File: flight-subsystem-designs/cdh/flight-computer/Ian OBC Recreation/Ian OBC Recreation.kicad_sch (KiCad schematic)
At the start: 43 parts, among them J1 Conn_01x03, J2 Conn_01x03, J3 Conn_01x03, J4 Conn_01x03, J5 Conn_01x03, J6 Conn_01x03, J8 Conn_02x26_Odd_Even, Q1 AON6411, U1 BEAGLEBONEBLACK, U2 TPS2400DBVR, U3 TCAN337G, U4 MCP7940N-xSN, U5 ADM3485EARZ, U6 MAX706RESA+T, U7 TMP36xS

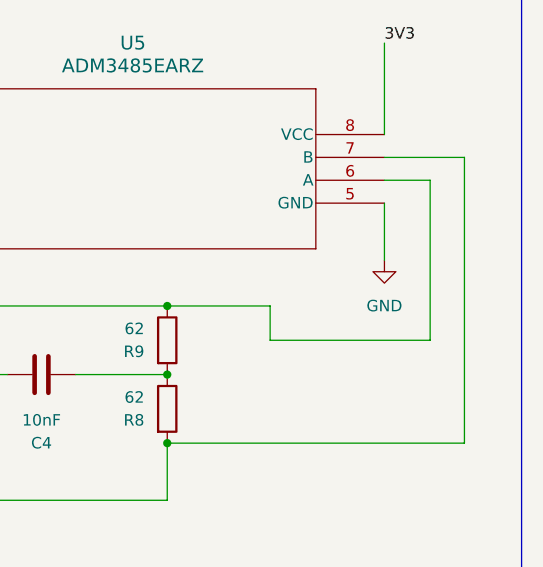
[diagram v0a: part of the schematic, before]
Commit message: Hashed down to warnings - Still not trustworthy
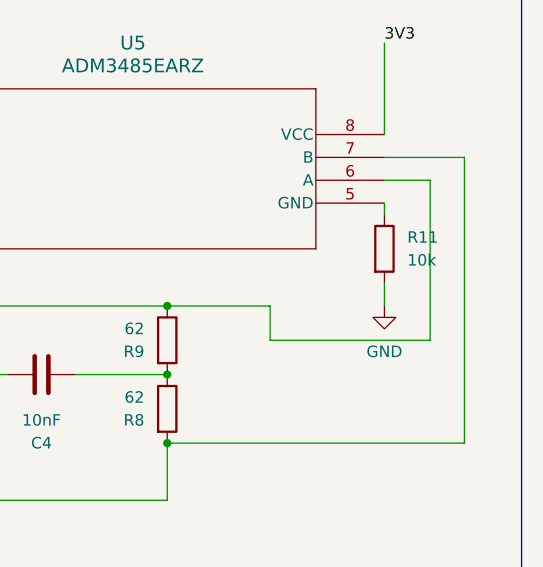
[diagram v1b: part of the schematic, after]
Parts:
- added R11: 10k, Resistor_SMD:R_0805_2012Metric_Pad1.20x1.40mm_HandSolder, symbol Device:R
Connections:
- net DGND: now also R11.2; no longer U5.5 (GND)
- new net: R11.1, U5.5 (GND)
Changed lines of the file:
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@@
 	(wire
 		(pts
+			(xy 384.81 139.7) (xy 384.81 142.24)
+		)
+		(stroke
+			(width 0)
+			(type default)
+		)
+	)
+	(wire
+		(pts
 			(xy 140.97 154.94) (xy 140.97 148.59)
 		)
@@
 	(wire
 		(pts
-			(xy 384.81 130.81) (xy 384.81 137.16)
+			(xy 384.81 130.81) (xy 384.81 132.08)
 		)
 		(stroke
@@
 	(symbol
 		(lib_id "power:GND")
-		(at 384.81 137.16 0)
+		(at 384.81 142.24 0)
 		(unit 1)
 		(exclude_from_sim no)
@@
 		(fields_autoplaced yes)
 		(property "Reference" "#PWR020"
-			(at 384.81 143.51 0)
+			(at 384.81 148.59 0)
 			(effects
 				(font
@@
 		)
 		(property "Value" "GND"
-			(at 384.81 142.24 0)
+			(at 384.81 147.32 0)
 			(effects
 				(font
@@
 		)
 		(property "Footprint" ""
-			(at 384.81 137.16 0)
+			(at 384.81 142.24 0)
 			(effects
 				(font
@@
 		)
 		(property "Datasheet" ""
-			(at 384.81 137.16 0)
+			(at 384.81 142.24 0)
 			(effects
 				(font
@@
 		)
 		(property "Description" "Power symbol creates a global label with name \"GND\" , ground"
-			(at 384.81 137.16 0)
+			(at 384.81 142.24 0)
 			(effects
 				(font
@@
 					(unit 1)
 				)
+			)
+		)
+	)
+	(symbol
+		(lib_id "Device:R")
+		(at 384.81 135.89 0)
+		(unit 1)
+		(exclude_from_sim no)
+		(in_bom yes)
+		(on_board yes)
+		(dnp no)
+		(fields_autoplaced yes)
+		(property "Reference" "R11"
+			(at 387.35 134.6199 0)
+			(effects
+				(font
+					(size 1.27 1.27)
+				)
+				(justify left)
+			)
+		)
+		(property "Value" "10k"
+			(at 387.35 137.1599 0)
+			(effects
+				(font
+					(size 1.27 1.27)
+				)
+				(justify left)
+			)
+		)
+		(property "Footprint" "Resistor_SMD:R_0805_2012Metric_Pad1.20x1.40mm_HandSolder"
+			(at 383.032 135.89 90)
+			(effects
+				(font
+					(size 1.27 1.27)
+				)
+				(hide yes)
+			)
+		)
+		(property "Datasheet" "~"
+			(at 384.81 135.89 0)
+			(effects
+				(font
+					(size 1.27 1.27)
+				)
+				(hide yes)
+			)
+		)
+		(property "Description" "Resistor"
+			(at 384.81 135.89 0)
+			(effects
+				(font
+					(size 1.27 1.27)
+				)
+				(hide yes)
+			)
+		)
+		(pin "1"
+		)
+		(pin "2"
+		)
+		(instances
+			(project ""
+				(path "/cd96c2b5-08b0-4094-8278-e7bcd71ae601"
+					(reference "R11")
+					(unit 1)
+				)

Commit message: Routing is fixed unless I missed something
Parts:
- removed J1, J2, J3, J4, J5, J6: Conn_01x03, Connector_PinHeader_2.54mm:PinHeader_1x03_P2.54mm_Vertical, symbol Connector_Generic:Conn_01x03
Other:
- note removed: "CAN"
- note removed: "I2C"
- note removed: "TEST POINTS"
- note removed: "Uart"

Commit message: Intermediate fixes, still WIP
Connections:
- net 5VIN is gone; now on net SYS_5V: J8.77 (Pin_25), J8.78 (Pin_26)
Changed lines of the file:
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@@
 		)
 	)
-	(label "5V"
+	(label "5VIN"
 		(at 95.25 16.51 0)
 		(effects

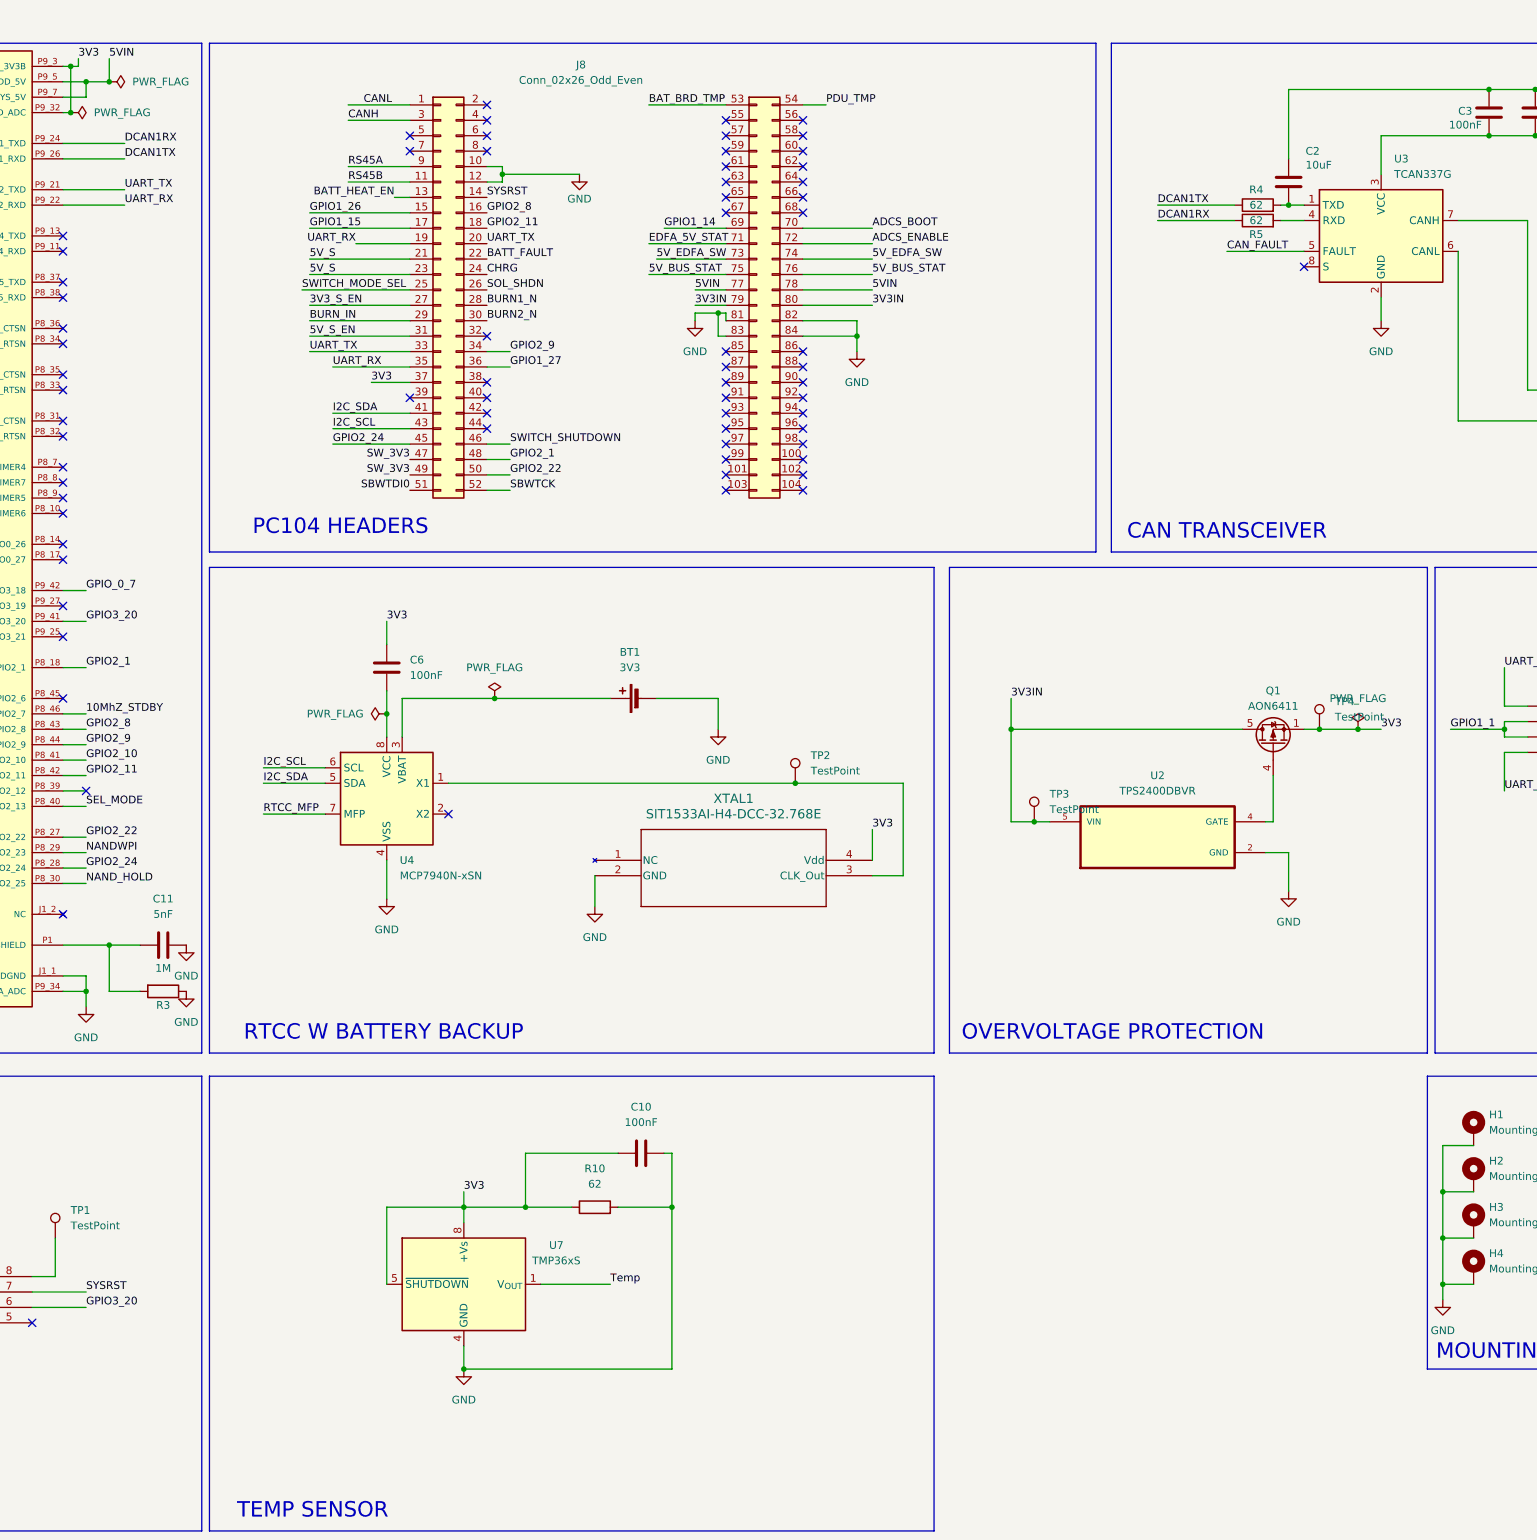
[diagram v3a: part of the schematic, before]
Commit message: Mounting holes still need work
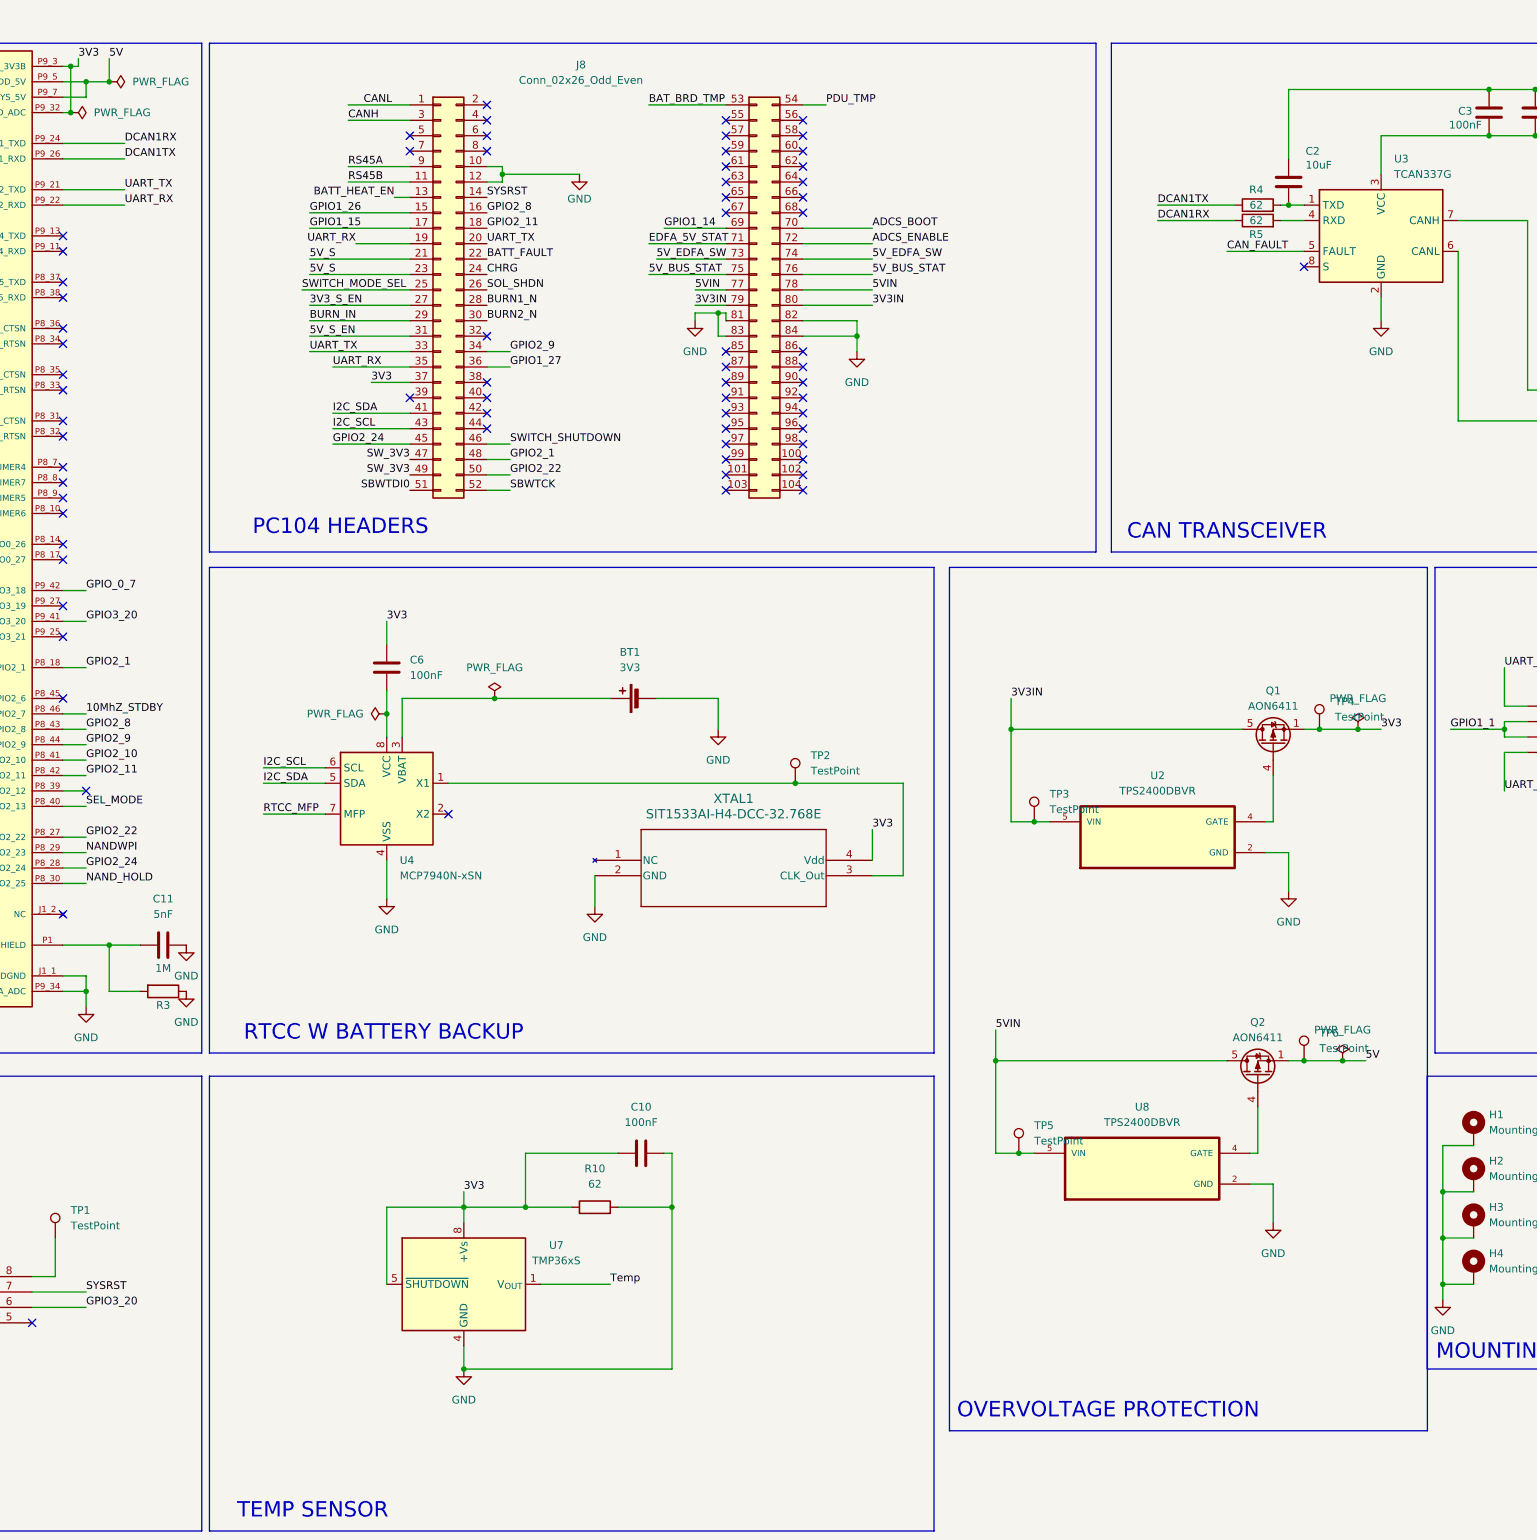
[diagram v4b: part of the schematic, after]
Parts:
- added Q2: AON6411, Package_DFN_QFN:AO_DFN-8-1EP_5.55x5.2mm_P1.27mm_EP4.12x4.6mm, symbol Transistor_FET:AON6411
- added TP5, TP6: TestPoint, TestPoint:TestPoint_THTPad_D3.0mm_Drill1.5mm, symbol Connector:TestPoint
- added U8: TPS2400DBVR, Footprints:SOT95P280X145-5N, symbol TPS2400DBVR:TPS2400DBVR
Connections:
- net DGND: now also U8.2 (GND)
- net SYS_5V: now also Q2.1 (S), Q2.2 (S), Q2.3 (S), TP6.1; no longer J8.77 (Pin_25), J8.78 (Pin_26)
- new net: Q2.4 (G), U8.4 (GATE)
- new net 5VIN: J8.77 (Pin_25), J8.78 (Pin_26), Q2.5 (D), TP5.1, U8.5 (VIN)

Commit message: Librecube Friendly Hopefully; Wiring Needs Work :C
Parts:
- removed J8: Conn_02x26_Odd_Even, Footprints:LibreCube_PC104_4x26_P2.54mm_adjacent, symbol PC104:Conn_02x26_Odd_Even
- added C12, C9: 10 uF, symbol Device:C
- added C7, C8: 100 nF, symbol Device:C
- added H5, H6: PC/104 Connector, Connector_PinSocket_2.54mm:PinSocket_2x26_P2.54mm_Vertical, symbol Connector_Generic:Conn_02x26_Odd_Even
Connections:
- net 3V3IN: now also C12.1, C8.1, H6.27 (Pin_27), H6.28 (Pin_28)
- net 3V3_S_EN: now also H5.27 (Pin_27)
- net 5VIN: now also C7.1, C9.1, H6.25 (Pin_25), H6.26 (Pin_26)
- net 5V_BUS_STAT: now also H6.23 (Pin_23), H6.24 (Pin_24)
- net 5V_EDFA_SW: now also H6.21 (Pin_21), H6.22 (Pin_22)
- net 5V_S: now also H5.21 (Pin_21), H5.23 (Pin_23)
- net 5V_S_EN: now also H5.31 (Pin_31)
- net ADCS_BOOT: now also H6.18 (Pin_18)
- net ADCS_ENABLE: now also H6.20 (Pin_20)
- net BATT_FAULT: now also H5.22 (Pin_22)
- net BATT_HEAT_EN: now also H5.13 (Pin_13)
- net BAT_BRD_TMP: now also H6.1 (Pin_1)
- net BURN1_N: now also H5.28 (Pin_28)
- net BURN2_N: now also H5.30 (Pin_30)
- net BURN_IN: now also H5.29 (Pin_29)
- net CANH: now also H5.3 (Pin_3)
- net CANL: now also H5.1 (Pin_1)
- net CHRG: now also H5.24 (Pin_24)
- net DGND: now also C12.2, C7.2, C8.2, C9.2, H5.10 (Pin_10), H5.12 (Pin_12), H6.29 (Pin_29), H6.30 (Pin_30), H6.31 (Pin_31), H6.32 (Pin_32)
- net EDFA_5V_STAT: now also H6.19 (Pin_19)
- net GPIO1_14: now also H6.17 (Pin_17)
- net GPIO1_15: now also H5.17 (Pin_17)
- net GPIO1_26: now also H5.15 (Pin_15)
- net GPIO1_27: now also H5.36 (Pin_36)
- net GPIO2_1: now also H5.48 (Pin_48)
- net GPIO2_11: now also H5.18 (Pin_18)
- net GPIO2_22: now also H5.50 (Pin_50)
- net GPIO2_24: now also H5.45 (Pin_45)
- net GPIO2_8: now also H5.16 (Pin_16)
- net GPIO2_9: now also H5.34 (Pin_34)
- net I2C_SCL: now also H5.43 (Pin_43)
- net I2C_SDA: now also H5.41 (Pin_41)
- net PDU_TMP: now also H6.2 (Pin_2)
- net RS45A: now also H5.9 (Pin_9)
- net RS45B: now also H5.11 (Pin_11)
- net SBWTCK: now also H5.52 (Pin_52)
- net SBWTDI0: now also H5.51 (Pin_51)
- net SOL_SHDN: now also H5.26 (Pin_26)
- net SWITCH_MODE_SEL: now also H5.25 (Pin_25)
- net SWITCH_SHUTDOWN: now also H5.46 (Pin_46)
- net SW_3V3: now also H5.47 (Pin_47), H5.49 (Pin_49)
- net SYSRST: now also H5.14 (Pin_14)
- net UART_RX: now also H5.19 (Pin_19), H5.35 (Pin_35)
- net UART_TX: now also H5.20 (Pin_20), H5.33 (Pin_33)
- net VDD_3V3B: now also H5.37 (Pin_37)
